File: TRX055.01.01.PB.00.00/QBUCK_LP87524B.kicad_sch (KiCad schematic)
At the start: 13 parts, among them U4 LP87524JRNFRQ1

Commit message: Update Layout
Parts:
- U4: JLCPCB Part # (none) -> C701982
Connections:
- net GND: now also U4.11 (PGND_B01), U4.17 (AGND), U4.24 (PGND_B23), U4.27 (AGND), U4.28 (AGND), U4.29 (AGND), U4.30 (AGND), U4.4 (AGND)
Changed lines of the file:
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@@
+	)
+	(junction
+		(at 153.67 121.92)
+		(diameter 0)
+		(color 0 0 0 0)
 	)
 	(junction
@@
 	)
 	(junction
+		(at 153.67 124.46)
+		(diameter 0)
+		(color 0 0 0 0)
+	)
+	(junction
 		(at 184.15 87.63)
 		(diameter 0)
@@
 	(wire
 		(pts
+			(xy 153.67 124.46) (xy 153.67 121.92)
+		)
+		(stroke
+			(width 0)
+			(type default)
+		)
+	)
+	(wire
+		(pts
 			(xy 97.79 111.76) (xy 109.22 111.76)
 		)
@@
 	(wire
 		(pts
+			(xy 153.67 127) (xy 153.67 124.46)
+		)
+		(stroke
+			(width 0)
+			(type default)
+		)
+	)
+	(wire
+		(pts
 			(xy 168.91 91.44) (xy 168.91 93.98)
 		)
@@
 	(wire
 		(pts
+			(xy 153.67 121.92) (xy 153.67 119.38)
+		)
+		(stroke
+			(width 0)
+			(type default)
+		)
+	)
+	(wire
+		(pts
 			(xy 177.8 120.65) (xy 184.15 120.65)
 		)
@@
 	(wire
 		(pts
+			(xy 149.86 121.92) (xy 153.67 121.92)
+		)
+		(stroke
+			(width 0)
+			(type default)
+		)
+	)
+	(wire
+		(pts
 			(xy 105.41 81.28) (xy 105.41 83.82)
 		)
@@
 	(wire
 		(pts
+			(xy 153.67 119.38) (xy 149.86 119.38)
+		)
+		(stroke
+			(width 0)
+			(type default)
+		)
+	)
+	(wire
+		(pts
 			(xy 195.58 120.65) (xy 195.58 124.46)
 		)
@@
 		(pts
 			(xy 168.91 101.6) (xy 149.86 101.6)
+		)
+		(stroke
+			(width 0)
+			(type default)
+		)
+	)
+	(wire
+		(pts
+			(xy 149.86 124.46) (xy 153.67 124.46)
 		)
 		(stroke
@@
 				(path "/6d8e09de-b00a-46e6-b61c-e43c092be287/4166cae5-8deb-4e8f-b2de-7cdde4d1a46f/f42c7148-2878-49bf-aa6d-96a73e74ef1c"
 					(reference "#PWR053")
+					(unit 1)
+				)
+			)
+		)
+	)
+	(symbol
+		(lib_id "power:GND")
+		(at 153.67 127 0)
+		(unit 1)
+		(exclude_from_sim no)
+		(in_bom yes)
+		(on_board yes)
+		(dnp no)
+		(property "Reference" "#PWR0133"
+			(at 153.67 133.35 0)
+			(effects
+				(font
+					(size 1.27 1.27)
+				)
+				(hide yes)
+			)
+		)
+		(property "Value" "GND"
+			(at 153.67 130.81 0)
+			(effects
+				(font
+					(size 1.27 1.27)
+				)
+			)
+		)
+		(property "Footprint" ""
+			(at 153.67 127 0)
+			(effects
+				(font
+					(size 1.27 1.27)
+				)
+				(hide yes)
+			)
+		)
+		(property "Datasheet" ""
+			(at 153.67 127 0)
+			(effects
+				(font
+					(size 1.27 1.27)
+				)
+				(hide yes)
+			)
+		)
+		(property "Description" "Power symbol creates a global label with name \"GND\" , ground"
+			(at 153.67 127 0)
+			(effects
+				(font
+					(size 1.27 1.27)
+				)
+				(hide yes)
+			)
+		)
+		(pin "1"
+		)
+		(instances
+			(project "TRX055.01.01.PB.00.00"
+				(path "/6d8e09de-b00a-46e6-b61c-e43c092be287/4166cae5-8deb-4e8f-b2de-7cdde4d1a46f/8784b81a-f0aa-4055-8508-d25cf4803403"
+					(reference "#PWR0133")
+					(unit 1)
+				)
+				(path "/6d8e09de-b00a-46e6-b61c-e43c092be287/4166cae5-8deb-4e8f-b2de-7cdde4d1a46f/f42c7148-2878-49bf-aa6d-96a73e74ef1c"
+					(reference "#PWR0134")
 					(unit 1)
 				)
@@
 				(hide yes)
 			)
+		)
+		(property "JLCPCB Part #" "C701982"
+			(at 129.54 99.06 0)
+			(effects
+				(font
+					(size 1.27 1.27)
+				)
+				(hide yes)
+			)

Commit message: +ETH +USB +Connectors
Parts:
- L1, L2, L3, L4: footprint Inductor_SMD:L_1008_2520Metric -> Resistor_SMD:R_01005_0402Metric
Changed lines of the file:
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@@
 			)
 		)
-		(property "Footprint" "Inductor_SMD:L_1008_2520Metric"
+		(property "Footprint" "Resistor_SMD:R_01005_0402Metric"
 			(at 161.29 113.03 0)
 			(effects
@@
 			)
 		)
-		(property "Footprint" "Inductor_SMD:L_1008_2520Metric"
+		(property "Footprint" "Resistor_SMD:R_01005_0402Metric"
 			(at 161.29 90.17 0)
 			(effects
@@
 			)
 		)
-		(property "Footprint" "Inductor_SMD:L_1008_2520Metric"
+		(property "Footprint" "Resistor_SMD:R_01005_0402Metric"
 			(at 161.29 105.41 0)
 			(effects
@@
 			)
 		)
-		(property "Footprint" "Inductor_SMD:L_1008_2520Metric"
+		(property "Footprint" "Resistor_SMD:R_01005_0402Metric"
 			(at 161.29 97.79 0)
 			(effects

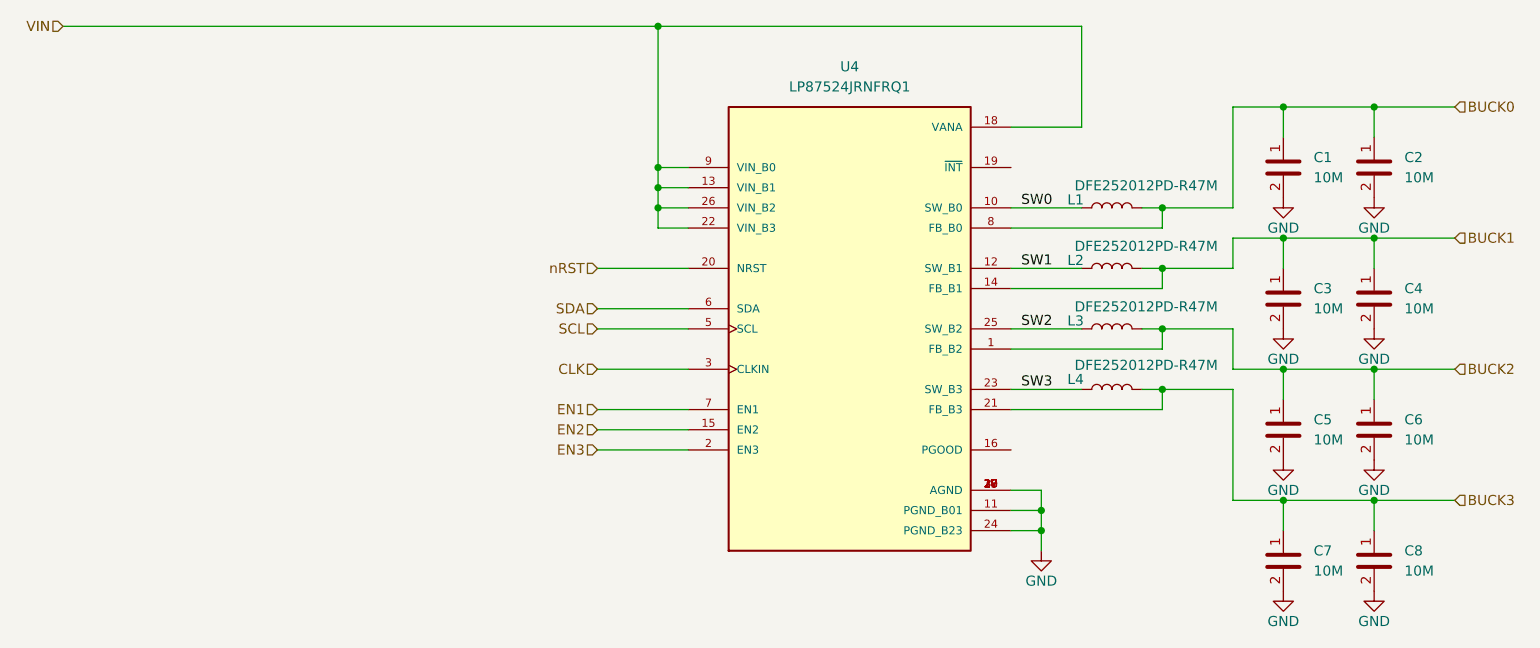
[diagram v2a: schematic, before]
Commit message: + add clocks + add PSU
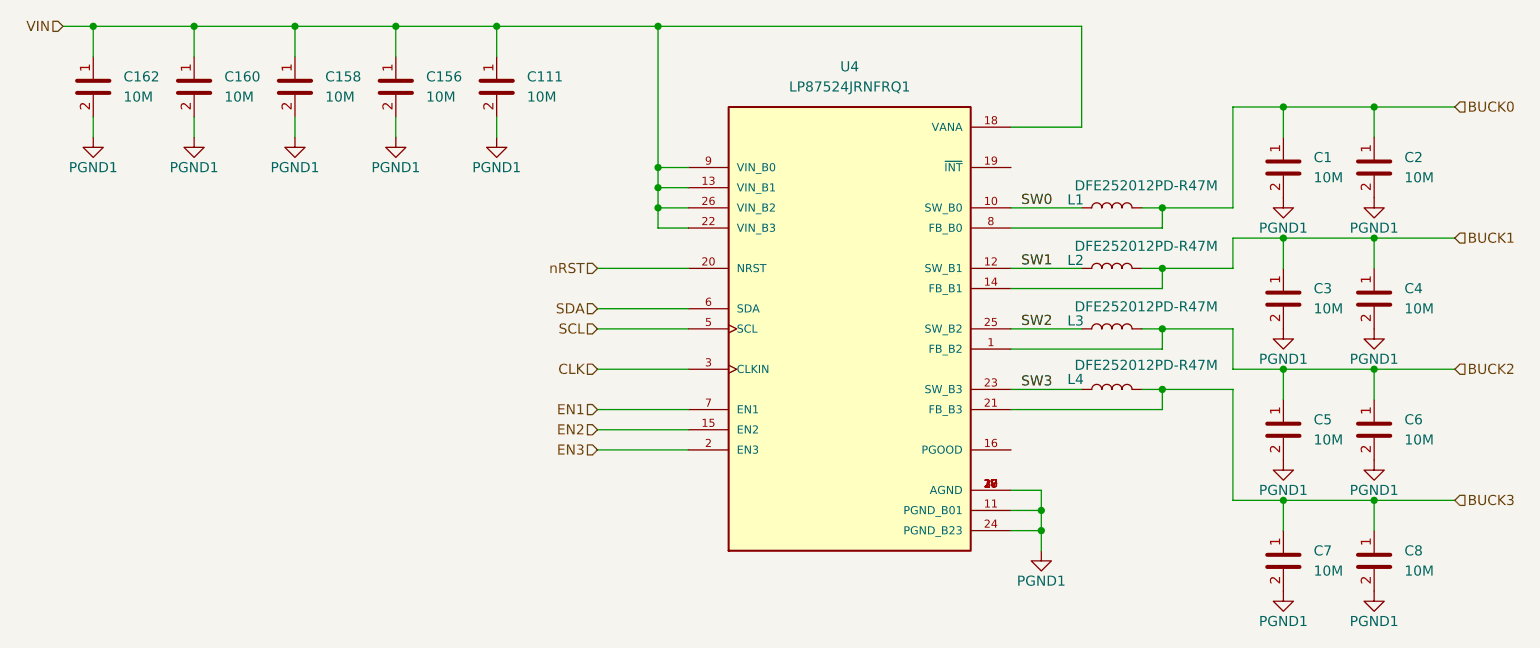
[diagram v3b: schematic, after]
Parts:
- added C111, C156, C158, C160, C162: 10M, Capacitor_SMD:C_0603_1608Metric, symbol PPA-Pasive:Cap
- C1, C2, C3, C4, C5, C6, C7, C8: JLCPCB Part # (none) -> C96446
- L1, L2, L3, L4: footprint Resistor_SMD:R_01005_0402Metric -> Inductor_SMD:L_1008_2520Metric; JLCPCB Part # (none) -> C1333867
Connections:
- net VIN: now also C111.1, C156.1, C158.1, C160.1, C162.1
- net GND renamed PGND1
- net PGND1: now also C111.2, C156.2, C158.2, C160.2, C162.2

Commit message: V0.1 - production, added brig-up comments
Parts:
- U4: footprint LP87524JRNFRQ1:VREG_LP87524JRNFRQ1 -> ppa-active:VREG_LP87524JRNFRQ1
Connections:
- net PGND1 renamed GND
- net GND: no longer U4.28 (AGND), U4.29 (AGND), U4.30 (AGND)
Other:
- company: (none) -> Tronex s.r.o. / Tronex Group USA LLC
- title: (none) -> TRNX SDR Carrier board
